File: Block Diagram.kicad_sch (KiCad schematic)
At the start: 0 parts

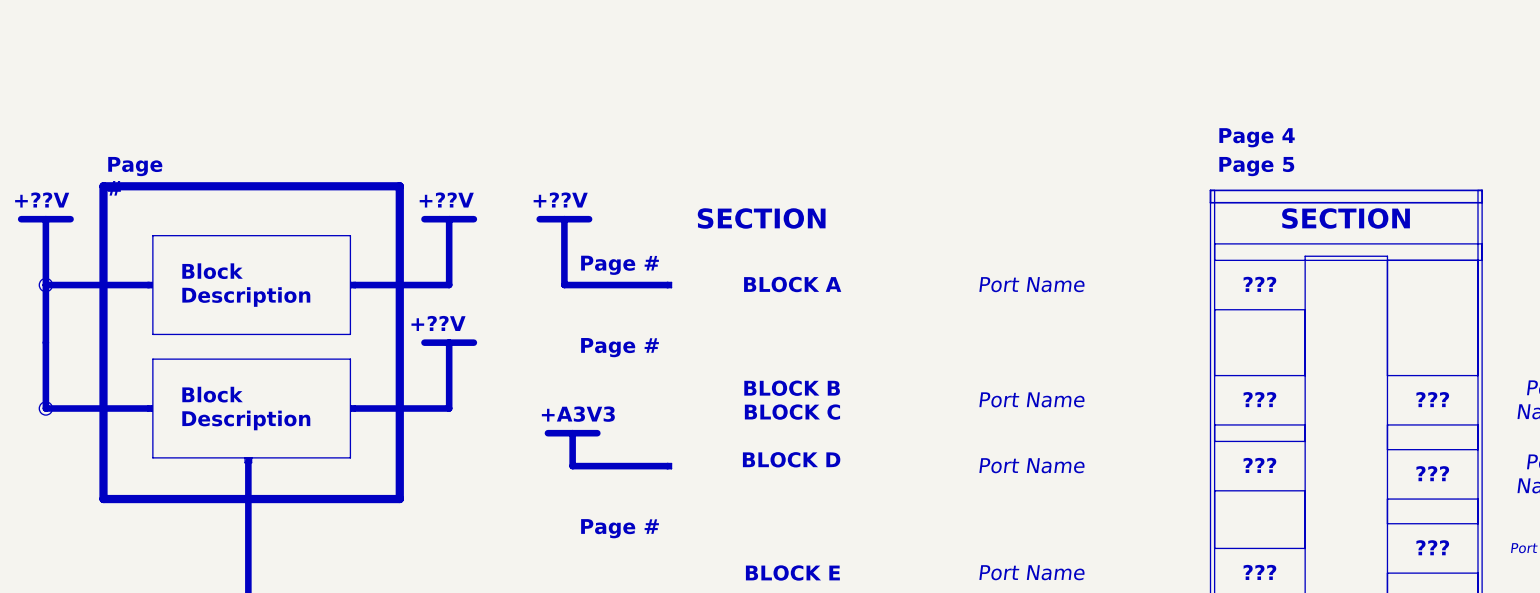
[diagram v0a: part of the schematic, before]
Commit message: minor updates of shematic and pcb and touch pad library
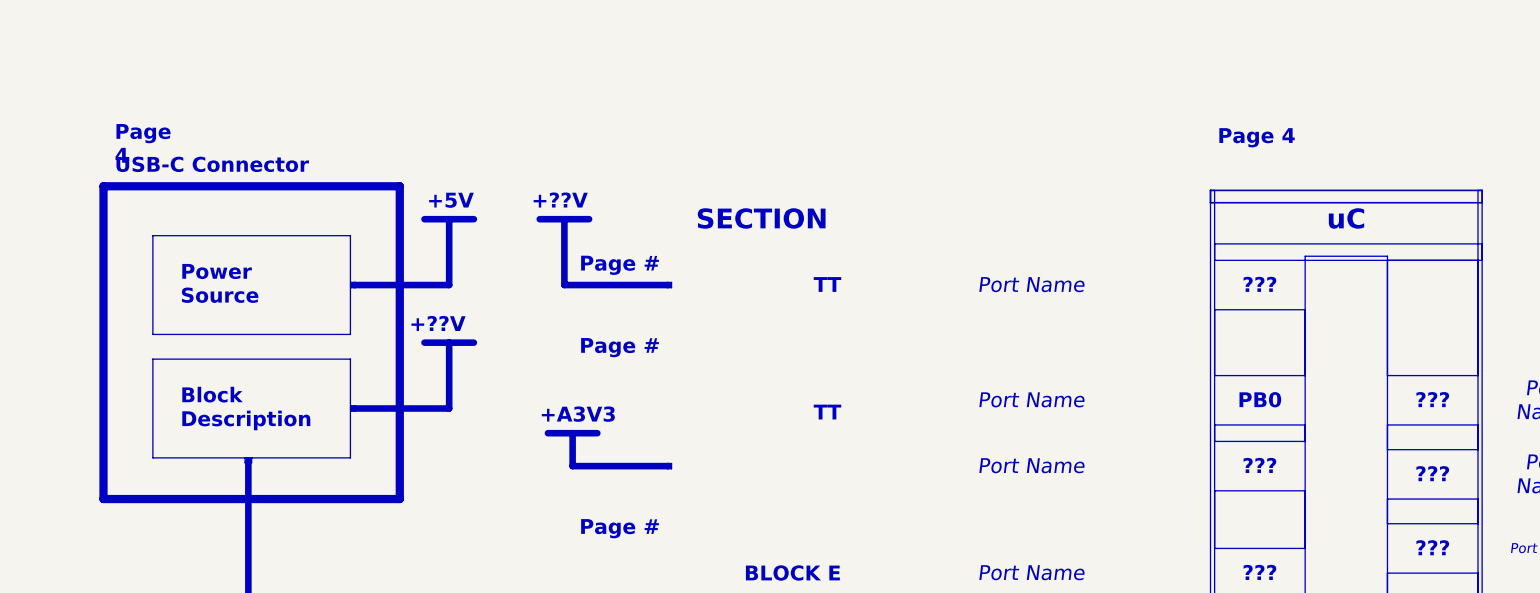
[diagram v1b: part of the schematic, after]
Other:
- note added: "+5V"
